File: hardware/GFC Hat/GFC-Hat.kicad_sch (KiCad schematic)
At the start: 37 parts, among them J1 BAT, U1 MAX17048G+T10, U2 BME280, U3 CAT24C32WI-GT3, U4 DS18B20

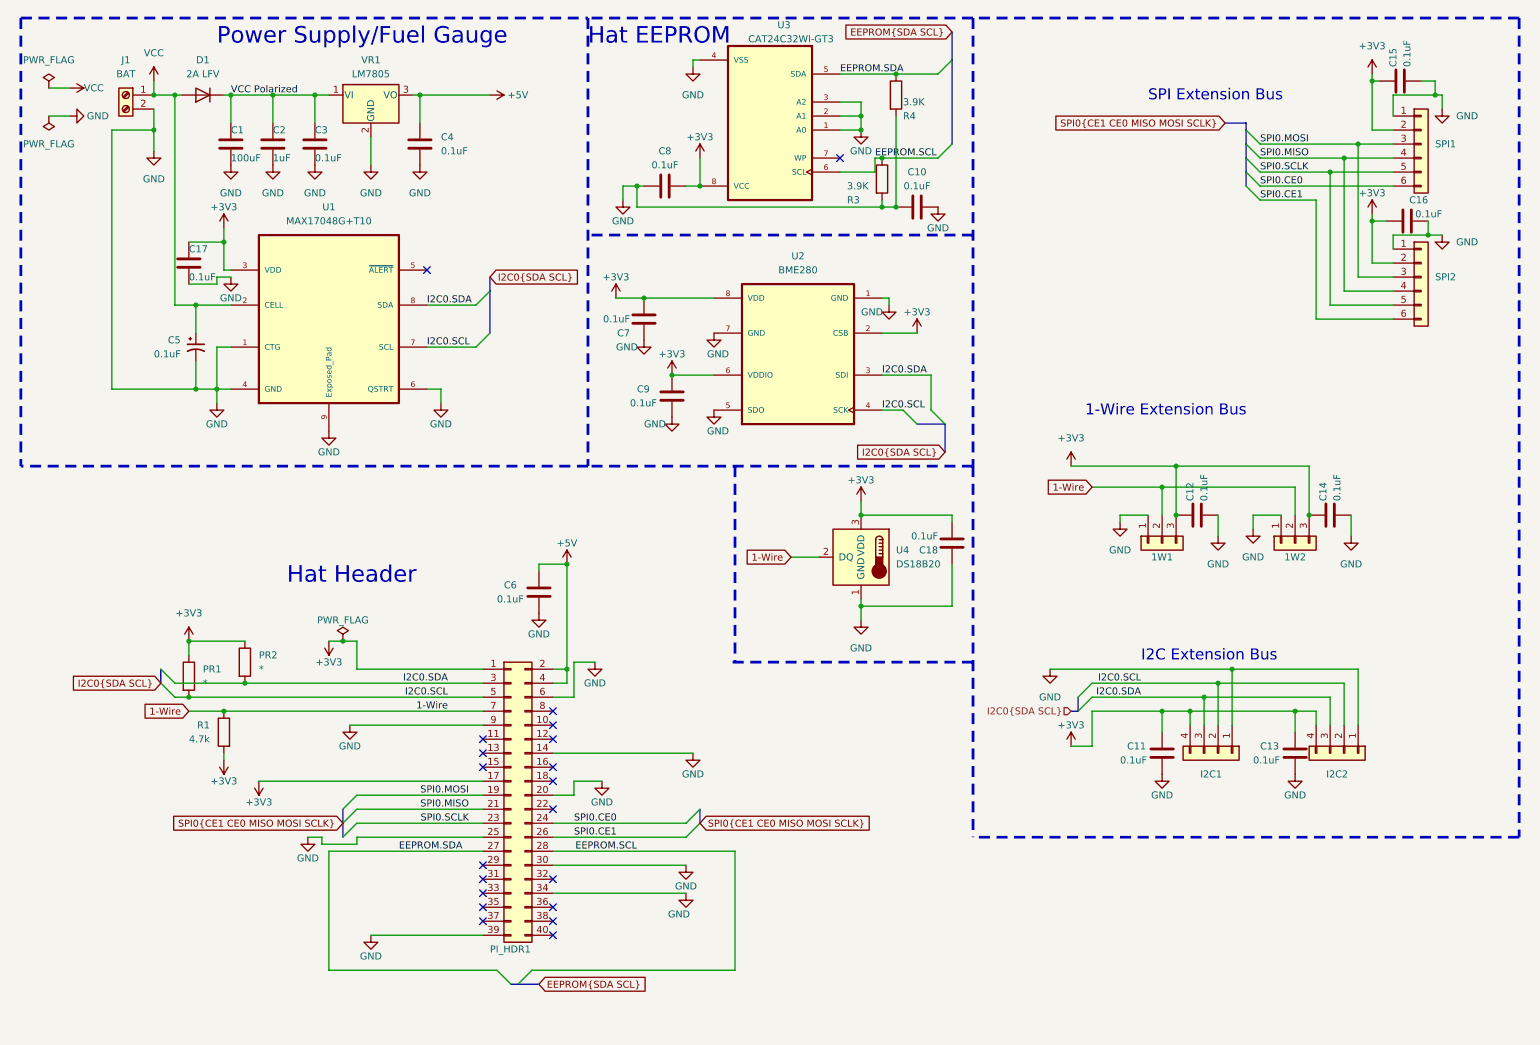
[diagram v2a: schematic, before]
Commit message: GFC Prototype 2 Complete and ordered - with BOM
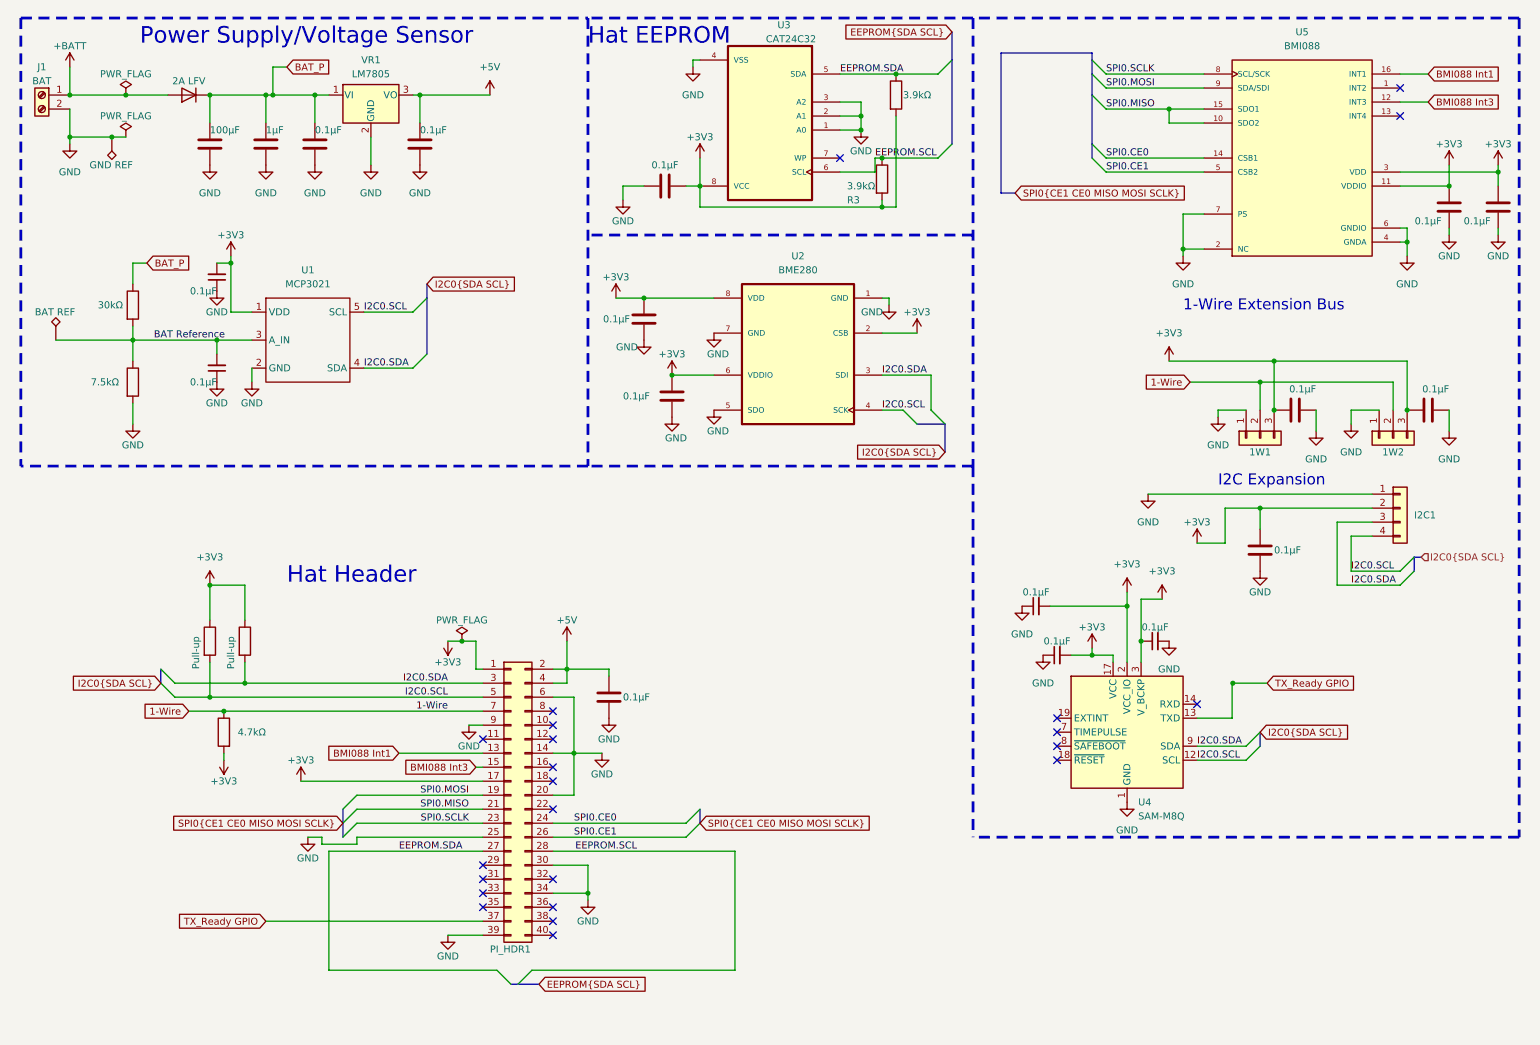
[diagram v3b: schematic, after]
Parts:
- removed C10, C16, C17, C18: 0.1uF, Capacitor_SMD:C_0603_1608Metric_Pad1.08x0.95mm_HandSolder, symbol Device:C
- removed C5: 0.1uF, Capacitor_SMD:C_0603_1608Metric_Pad1.08x0.95mm_HandSolder, symbol Device:C_Polarized_Small_US
- removed I2C2: I2C0, GFC-Hat-Footprints:JST_PH_B4B-PH-K_1x04_P2.00mm_Vertical, symbol Connector_Generic:Conn_01x04
- removed SPI1, SPI2: SPI, GFC-Hat-Footprints:JST_PH_B6B-PH-K_1x06_P2.00mm_Vertical, symbol Connector_Generic:Conn_01x06
- removed U1: MAX17048G+T10, MAX17048G_T10:SON50P200X200X80-9N, symbol GFC-Symbols:MAX17048G+T10
- removed U4: DS18B20, Package_TO_SOT_THT:TO-92_Inline, symbol Sensor_Temperature:DS18B20
- added C10, C17, C18, C19, C5: 0.1µF, Capacitor_SMD:C_0603_1608Metric, symbol Device:C_Small
- added R2: 30kΩ, Resistor_SMD:R_0603_1608Metric, symbol Device:R
- added R5: 7.5kΩ, Resistor_SMD:R_0603_1608Metric, symbol Device:R
- added TP1: GND REF, TestPoint:TestPoint_Keystone_5019_Minature, symbol Connector:TestPoint_Alt
- added TP2: BAT REF, TestPoint:TestPoint_Pad_D1.5mm, symbol Connector:TestPoint_Alt
- added U1: MCP3021, Package_TO_SOT_SMD:SOT-23-5, symbol GFC-Symbols:MCP3021
- added U4: SAM-M8Q, RF_GPS:ublox_SAM-M8Q, symbol RF_GPS:SAM-M8Q
- added U5: BMI088, PQFN50P450X300X100-16N, symbol GFC-Symbols:BMI088
- 1W1, 1W2: value 1-Wire Bus -> 1-Wire; footprint GFC-Hat-Footprints:JST_PH_B3B-PH-K_1x03_P2.00mm_Vertical -> Connector_PinHeader_1.27mm:PinHeader_1x03_P1.27mm_Vertical; DESCRIPTION JST B3B-PH-K-S -> Breakaway Header; Digikey https://www.digikey.com/en/products/detail/jst-sales-americ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 -> https://www.digikey.com/short/mwpz3z87
- C1: value 100uF -> 100µF; DESCRIPTION (none) -> A768EB107M1ELAS036; Digikey (none) -> https://www.digikey.com/short/nt5bcn78
- C11, C12, C14, C3, C4, C6, C7, C8, C9: value 0.1uF -> 0.1µF; footprint Capacitor_SMD:C_0603_1608Metric_Pad1.08x0.95mm_HandSolder -> Capacitor_SMD:C_0603_1608Metric; DESCRIPTION (none) -> CL10B104KB8NNWC; Digikey (none) -> https://www.digikey.com/short/dz14934f
- C13, C15: value 0.1uF -> 0.1µF; footprint Capacitor_SMD:C_0603_1608Metric_Pad1.08x0.95mm_HandSolder -> Capacitor_SMD:C_0603_1608Metric; DESCRIPTION (none) -> CL10B104KB8NNWC; Digikey (none) -> https://www.digikey.com/short/dz14934f; Unit Price (none) -> 0.10
- C2: value 1uF -> 1µF; footprint Capacitor_SMD:C_0805_2012Metric_Pad1.18x1.45mm_HandSolder -> Capacitor_SMD:C_0805_2012Metric
- D1: footprint Diode_SMD:D_SMA_Handsoldering -> Diode_SMD:D_SMA; DESCRIPTION (none) -> B320A-13-F; Digikey (none) -> https://www.digikey.com/short/z4nj92r1
- I2C1: value I2C0 -> I²C; footprint GFC-Hat-Footprints:JST_PH_B4B-PH-K_1x04_P2.00mm_Vertical -> Connector_PinHeader_1.27mm:PinHeader_1x04_P1.27mm_Vertical; DESCRIPTION JST B4B-PH-K-S -> Breakaway Header; Digikey https://www.digikey.com/en/products/detail/jst-sales-americ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 -> https://www.digikey.com/short/mwpz3z87
- J1: footprint GFC-Hat-Footprints:OSTVN02A150 2x1 Terminal Block -> GFC-Footprints:OSTVN02A150 2x1 Terminal Block; DESCRIPTION (none) -> OSTVN02A150; Digikey https://www.digikey.com/short/tr2hdfmv -> https://www.digikey.com/short/5mwt13md
- PI_HDR1: value PI Header -> PI; DESCRIPTION (none) -> Extended Header; Digikey (none) -> https://www.digikey.com/short/14zjphrn
- PR1, PR2: value * -> Pull-up; DESCRIPTION (none) -> Optional; Digikey (none) -> N/A
- R1: value 4.7k -> 4.7kΩ; footprint Resistor_SMD:R_0603_1608Metric_Pad0.98x0.95mm_HandSolder -> Resistor_SMD:R_0603_1608Metric; DESCRIPTION (none) -> RC0603JR-074K7L
- R3, R4: value 3.9K -> 3.9kΩ; footprint Resistor_SMD:R_0603_1608Metric_Pad0.98x0.95mm_HandSolder -> Resistor_SMD:R_0603_1608Metric; DESCRIPTION (none) -> RN73H1JTTD3701B25; Digikey (none) -> https://www.digikey.com/short/54rvbn8w
- U2: DESCRIPTION Integrated pressure, humidity and temperature sensor; 8-pin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 -> (none); Digikey (none) -> https://www.digikey.com/short/pjf7tjwh
- U3: value CAT24C32WI-GT3 -> CAT24C32
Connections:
- net +3V3: now also I2C1.2 (Pin_2), R3.2, R4.2, C10.2, C18.2, C19.1, C5.2, U1.1 (VDD), U4.17 (VCC), U4.2 (VCC_IO), U4.3 (V_BCKP), U5.11 (VDDIO), U5.3 (VDD); no longer I2C1.4 (Pin_4)
- net GND: now also C10.1, C17.1, C18.1, C19.2, C5.1, R5.2, TP1.1, U1.2 (GND), U4.1 (GND), U4.10 (GND), U4.11 (GND), U4.15 (GND), U4.16 (GND), U4.20 (GND), U4.4 (GND), U4.5 (GND), U4.6 (GND), U5.2 (NC), U5.4 (GNDA), U5.6 (GNDIO), U5.7 (PS); no longer R3.2, R4.2
- net I2C0.SCL: now also I2C1.4 (Pin_4), U1.5 (SCL), U4.12 (SCL); no longer I2C1.2 (Pin_2)
- net I2C0.SDA: now also U1.4 (SDA), U4.9 (SDA)
- net SPI0.CE0: now also U5.14 (CSB1)
- net SPI0.CE1: now also U5.5 (CSB2)
- net SPI0.MISO: now also U5.10 (SDO2), U5.15 (SDO1)
- net SPI0.MOSI: now also U5.9 (SDA/SDI)
- net SPI0.SCLK: now also U5.8 (SCL/SCK)
- net BMI088 Int1: now reaches PI_HDR1.13 (Pin_13)
- net BMI088 Int1: now also U5.16 (INT1)
- net BMI088 Int3: now reaches PI_HDR1.15 (Pin_15)
- net BMI088 Int3: now also U5.12 (INT3)
- net TX_Ready GPIO: now reaches PI_HDR1.37 (Pin_37)
- net TX_Ready GPIO: now also U4.13 (TXD)
- net VCC renamed +BATT
- net VCC Polarized renamed BAT_P
- net BAT_P: now also R2.1
- new net BAT Reference: C17.2, R2.2, R5.1, TP2.1, U1.3 (A_IN)
- no-connect marks 20 -> 23
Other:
- note added: "I2C Expansion"
- note added: "Power Supply/Voltage Sensor"
- note removed: "I2C Extension Bus"
- note removed: "Power Supply/Fuel Gauge"
- note removed: "SPI Extension Bus"
- moved on the sheet: 1W1, 1W2, I2C1, J1

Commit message: Schematic update
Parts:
- removed C7, C9: 0.1µF, Capacitor_SMD:C_0603_1608Metric, symbol Device:C
- removed PR1, PR2: Pull-up, Resistor_SMD:R_0603_1608Metric_Pad0.98x0.95mm_HandSolder, symbol Device:R
- removed R1: 4.7kΩ, Resistor_SMD:R_0603_1608Metric, symbol Device:R
- removed R3, R4: 3.9kΩ, Resistor_SMD:R_0603_1608Metric, symbol Device:R
- added C? (x2): 0.1µF, Capacitor_SMD:C_0603_1608Metric, symbol Device:C
- added R? (x2): 3.9kΩ, Resistor_SMD:R_0603_1608Metric, symbol Device:R
- added R?: 4.7kΩ, Resistor_SMD:R_0603_1608Metric, symbol Device:R
- added R? (x2): *, Resistor_SMD:R_0603_1608Metric, symbol Device:R
- PI_HDR1: symbol Connector_Generic:Conn_02x20_Odd_Even -> Connector:Raspberry_Pi_2_3
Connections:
- net +3V3: now also U2.3 (SDI), C?.2, C?.2, R?.1, R?.1, R?.1, R?.1, R?.2; no longer U2.2 (CSB)
- net +5V: now also C6.2; no longer C6.1
- net 1-Wire: now also R?.2
- net BAT_P: no longer R2.1
- net BMI088 Int1: now also PI_HDR1.33 (PWM1/GPIO13); no longer PI_HDR1.13 (Pin_13)
- net EEPROM.SCL: now also R?.2
- net EEPROM.SDA: now also R?.2
- net GND: now also C6.1, U2.2 (CSB), C?.1, C?.1; no longer C6.2, U2.1 (GND)
- net I2C0.SCL: now also U2.1 (GND), R?.1; no longer U2.4 (SCK)
- net I2C0.SDA: now also U2.4 (SCK), R?.2; no longer U2.3 (SDI)
- net BAT Reference renamed BAT Reference Voltage
- net TX_Ready GPIO renamed GPS TX-Ready
- net GPS TX-Ready: no longer PI_HDR1.37 (Pin_37)
- new net BAT Polarized: R2.1
- new net GPS TxReady: PI_HDR1.37 (GPIO26)
- no-connect marks 23 -> 12
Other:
- note added: "Optional Pull-Up Resistors May not be needed due to internal pull-ups depending on device/wires added to the I2C header."
- note added: "Power Supply"
- note added: "Pressure/Temperature/Humidity Sensor"
- note added: "Reserved For DRA818"
- note added: "Voltage Sensor - (I2C ADC)"
- note removed: "Hat Header"
- note removed: "Power Supply/Voltage Sensor"
- moved on the sheet: U1, U2, U3

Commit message: Schematic update
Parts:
- gave numbers to parts that had none: 7
- renumbered C8 to C10, C13 to C11, C15 to C12, C14 to C13, C11 to C14, C18 to C15, C10 to C16, C19 to C17, C6 to C5, C5 to C6, C17 to C7, R2 to R1, R5 to R2
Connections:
- net +3V3: now also C14.1, U2.2 (CSB); no longer C14.2, U2.3 (SDI)
- net GND: now also C14.2, U2.1 (GND); no longer C14.1, U2.2 (CSB)
- net I2C0.SCL: now also I2C1.3 (Pin_3), U2.4 (SCK); no longer I2C1.4 (Pin_4), U2.1 (GND)
- net I2C0.SDA: now also I2C1.4 (Pin_4), U2.3 (SDI); no longer I2C1.3 (Pin_3), U2.4 (SCK)
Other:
- note added: "1-Wire Expansion"
- note added: "GPS"
- note added: "IMU"
- note added: "Pi Header"
- note removed: "1-Wire Extension Bus"
- company: (none) -> Joshua Jerred
- moved on the sheet: 1W1, 1W2, I2C1, PI_HDR1, U4, U5

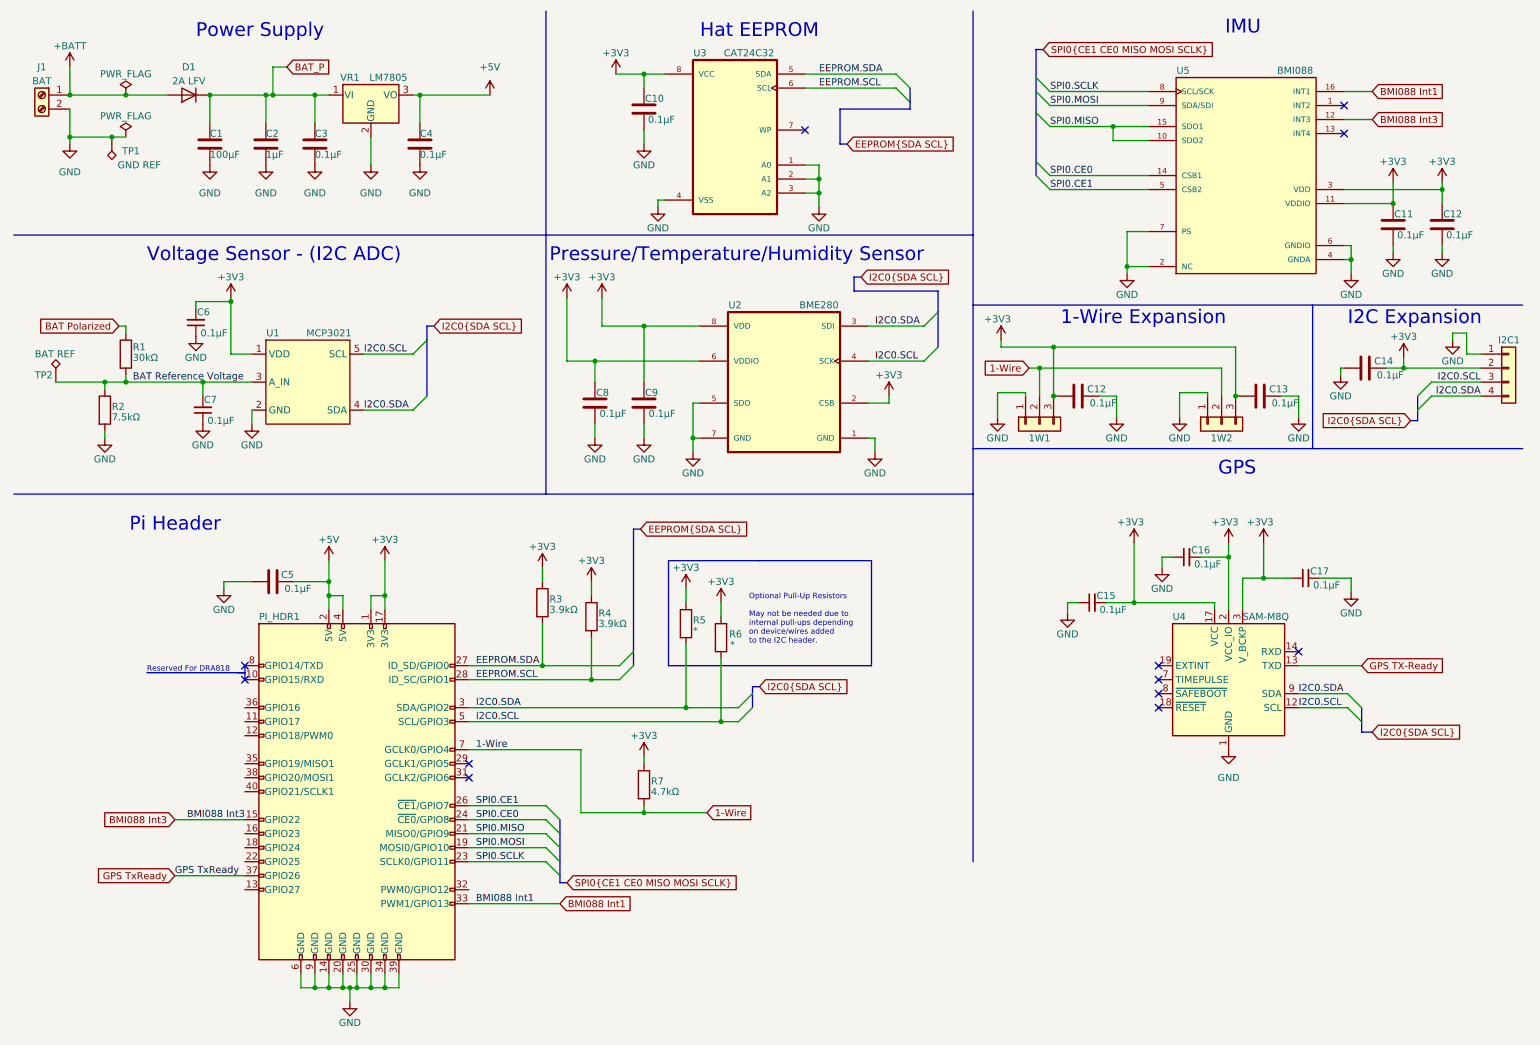
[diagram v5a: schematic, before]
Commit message: Hardware update to bring it up to KiCad 7.0
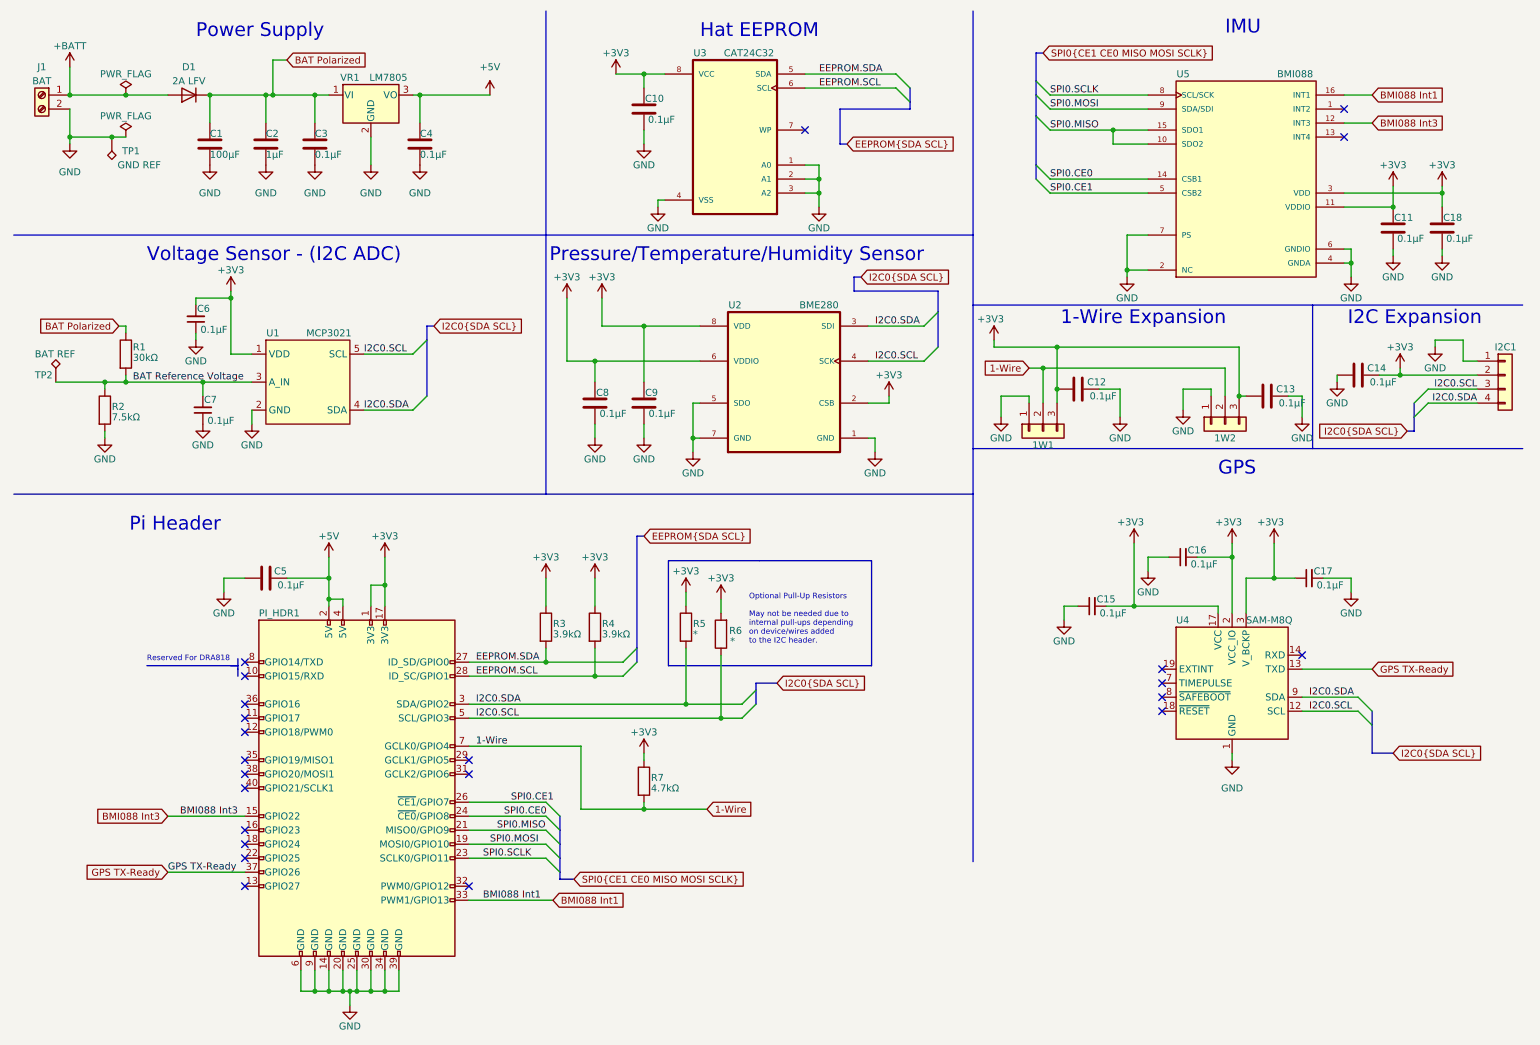
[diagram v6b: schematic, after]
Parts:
- renumbered C12 to C18
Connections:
- net BAT_P is gone; now on net BAT Polarized: C1.1, C2.1, C3.1, D1.1 (K), VR1.1 (VI)
- net GPS TxReady is gone; now on net GPS TX-Ready: PI_HDR1.37 (GPIO26)
- no-connect marks 12 -> 23
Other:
- moved on the sheet: 1W1, 1W2, C11, C12, C13, C14, C15, C16, C17, C18, C5, C6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

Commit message: hardware updates
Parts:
- removed C1: 100µF, Capacitor_SMD:C_Elec_6.3x7.7, symbol Device:C
- removed C2: 1µF, Capacitor_SMD:C_0805_2012Metric, symbol Device:C
- removed C3, C4: 0.1µF, Capacitor_SMD:C_0603_1608Metric, symbol Device:C
- removed C6, C7: 0.1µF, Capacitor_SMD:C_0603_1608Metric, symbol Device:C_Small
- removed D1: 2A LFV, Diode_SMD:D_SMA, symbol GFC-Symbols:1N5400
- removed J1: BAT, GFC-Footprints:OSTVN02A150 2x1 Terminal Block, symbol Connector:Screw_Terminal_01x02
- removed R1: 30kΩ, Resistor_SMD:R_0603_1608Metric, symbol Device:R
- removed R2: 7.5kΩ, Resistor_SMD:R_0603_1608Metric, symbol Device:R
- removed TP1: GND REF, TestPoint:TestPoint_Keystone_5019_Minature, symbol Connector:TestPoint_Alt
- removed TP2: BAT REF, TestPoint:TestPoint_Pad_D1.5mm, symbol Connector:TestPoint_Alt
- removed U1: MCP3021, Package_TO_SOT_SMD:SOT-23-5, symbol GFC-Symbols:MCP3021
- removed VR1: LM7805, Package_TO_SOT_SMD:TO-263-3_TabPin2, symbol GFC-Symbols:LM7805_TO220
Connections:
- net GPS Reset Pin: now reaches U4.18 (~{RESET})
- no-connect marks 23 -> 22
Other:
- added sheet power_supply (power_supply.kicad_sch)
- note removed: "Power Supply"
- note removed: "Voltage Sensor - (I2C ADC)"
